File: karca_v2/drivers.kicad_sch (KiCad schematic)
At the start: 15 parts, among them J10 Keyhole ignition switch, J11 Screw_Terminal_01x04, J12 Buzzer, J9 Screw_Terminal_01x10, Q3 IRF3708

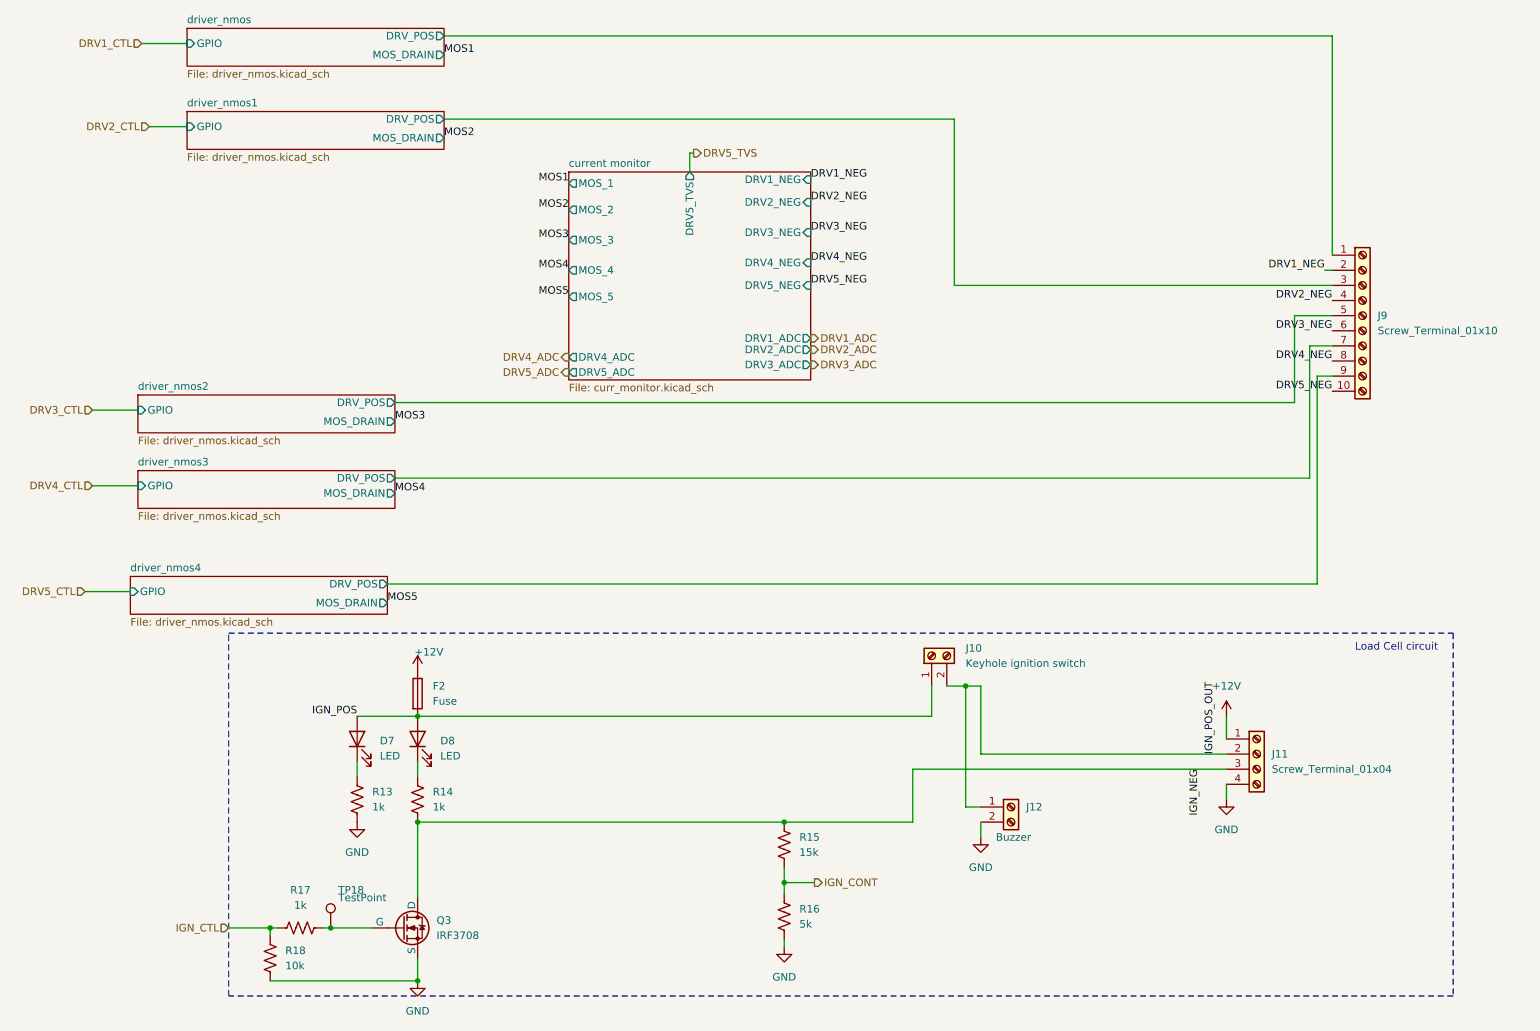
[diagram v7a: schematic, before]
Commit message: cleaned up documentation. Added production files and BOM. Marked Thermocouple components and THT components as DNP (excluded them from BOM too) to match version sent to JLCPCB for fabrication
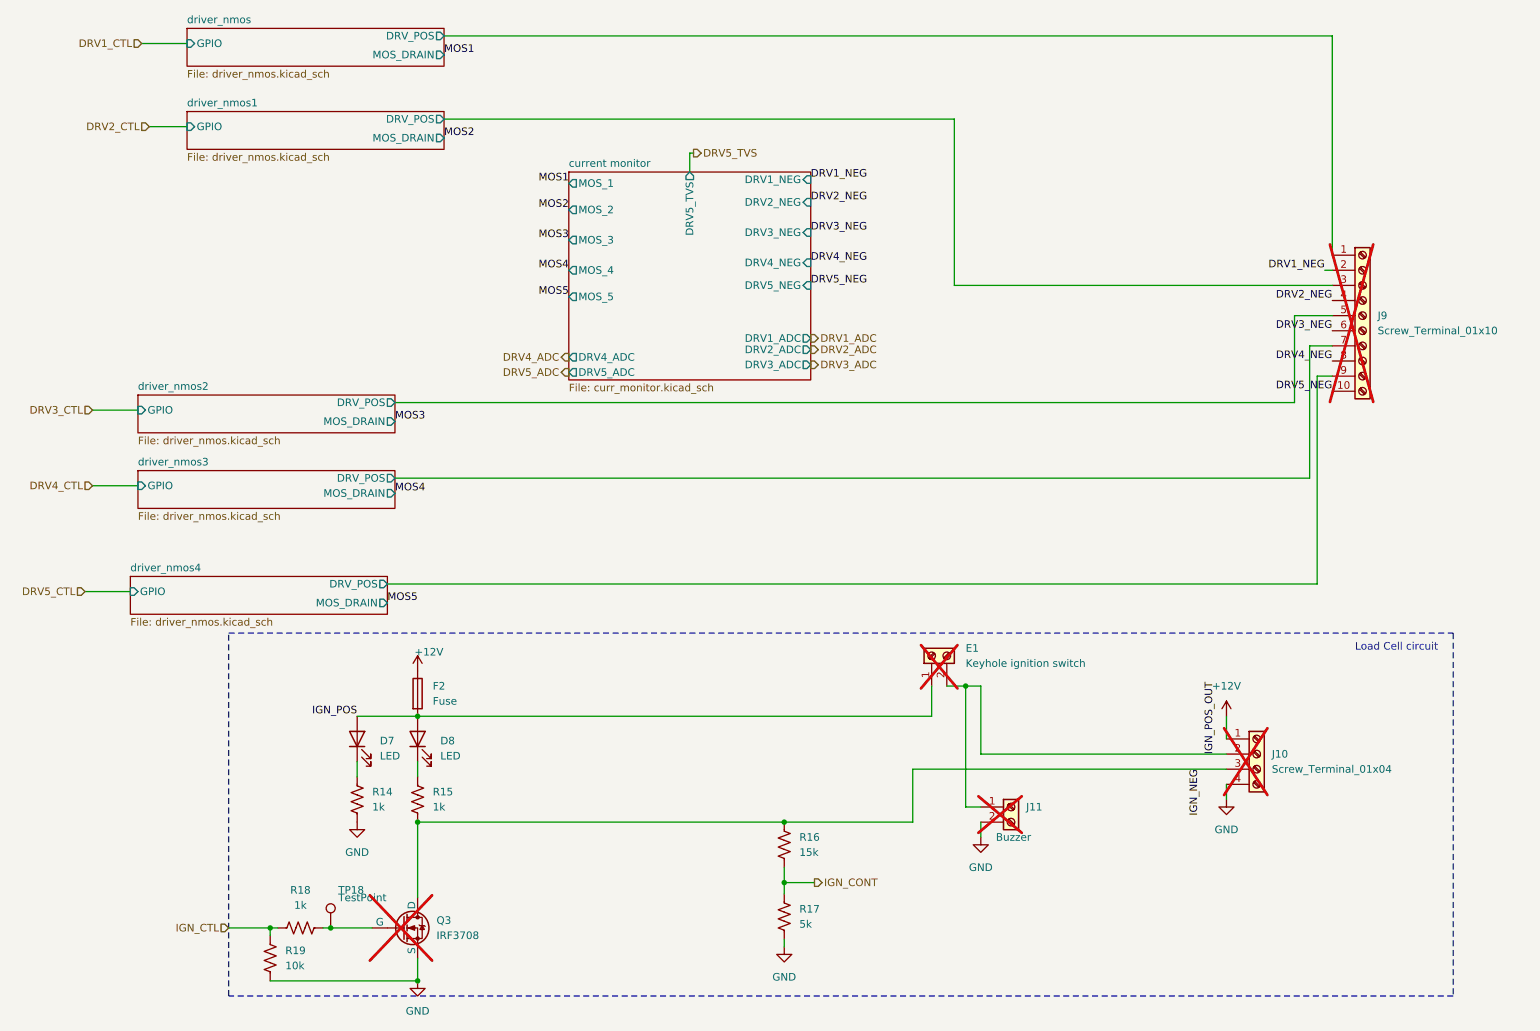
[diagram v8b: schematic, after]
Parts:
- D7: LCSC (none) -> C125084
- D8: LCSC (none) -> C14641
- E1: renamed from J10; now not fitted; now left out of the parts list
- F2: LCSC (none) -> C55996
- J10: renamed from J11; now not fitted; now left out of the parts list
- J11: renamed from J12; now not fitted; now left out of the parts list
- J9: now not fitted; now left out of the parts list
- Q3: footprint IRF3708:TO254P1041X444X1930-3 -> Package_TO_SOT_THT:TO-220-3_Vertical; now not fitted; now left out of the parts list
- renumbered R13 to R14, R14 to R15, R15 to R16, R16 to R17, R17 to R18, R18 to R19
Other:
- company: (none) -> Rice Eclipse
- title: (none) -> kARCA 2.0 Engine Control System
